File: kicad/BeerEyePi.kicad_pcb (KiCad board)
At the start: 2 copper layers, 65 x 63 mm, 72 parts, among them J1 RaspberryPi, J2 Extension, J3 RGB_LED, J4 TransSensor, J5 RGB_LED, J6 RGB_LED, J7 TransSensor, Q1 IRLML2502, Q2 IRLML2502, Q3 IRLML2502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

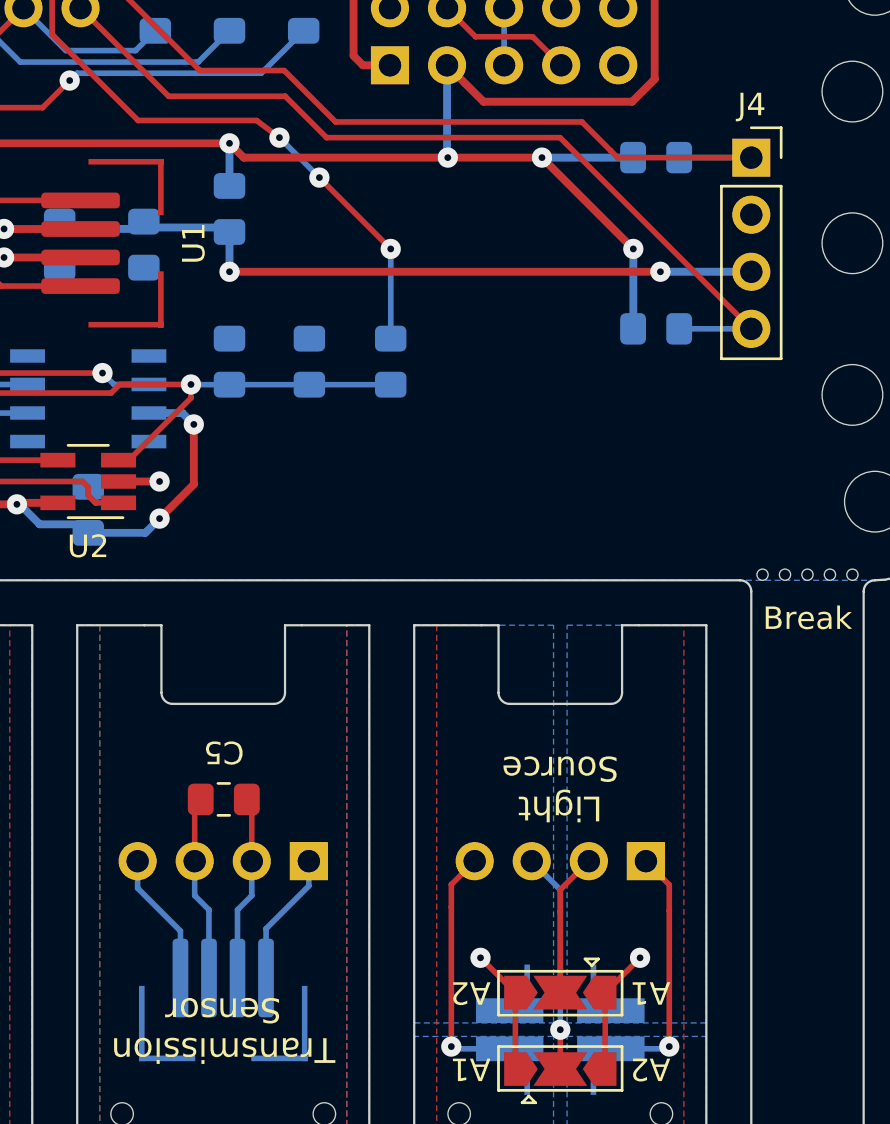
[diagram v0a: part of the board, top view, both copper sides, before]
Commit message: Fixed flawed pin socket orientation for sensor module. Generated gerber files.
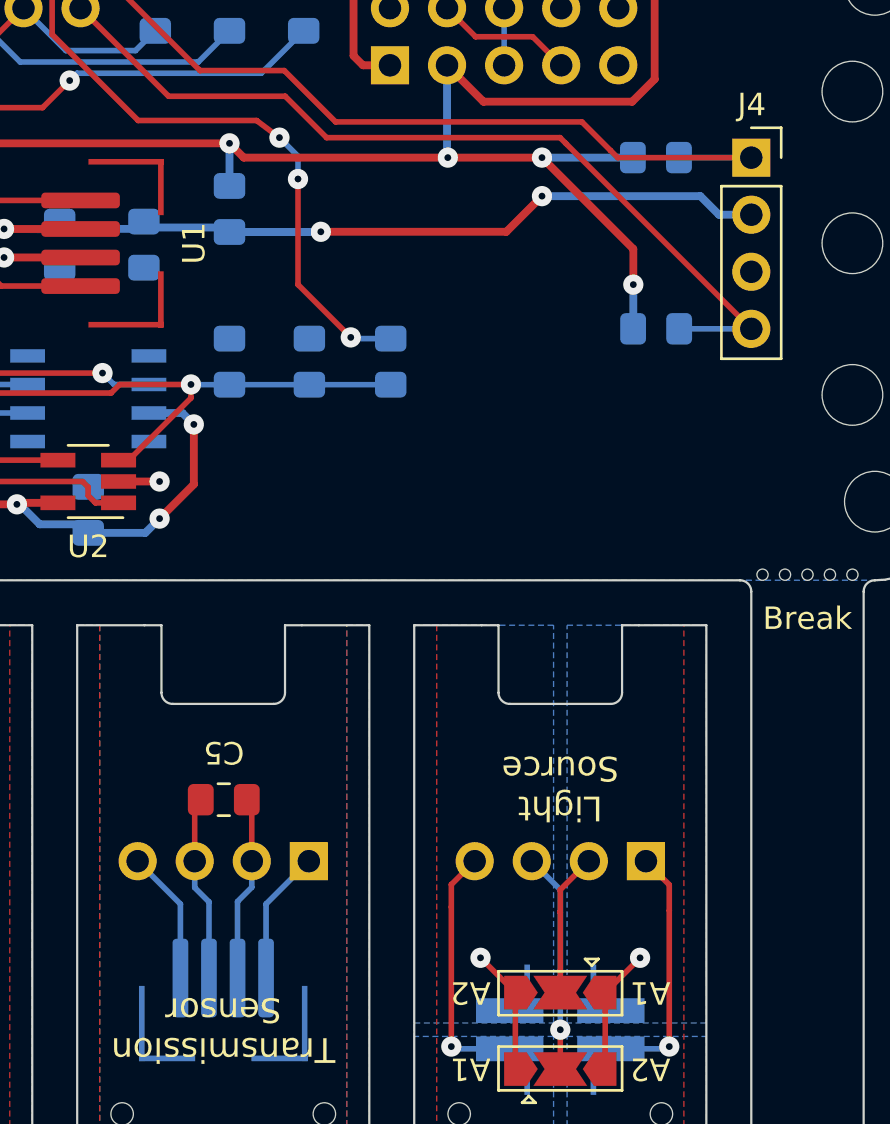
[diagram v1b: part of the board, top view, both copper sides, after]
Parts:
- moved R12 7.62 mm to (151.8, 111.2)
- moved R10 7.62 mm to (151.8, 118.8)
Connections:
- J1 pad 15: SCL1 -> SDA1
- J1 pad 16: SDA1 -> SCL1
- J4 pad 1: SDA1 -> SCL1
- J4 pad 2: GND -> +3.3VADC
- J4 pad 3: +3.3VADC -> GND
- J4 pad 4: SCL1 -> SDA1
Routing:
- net +3.3VADC: track 39.4 -> 42.7 mm
- net SDA1: track 36.9 -> 39.0 mm
- net SCL1: track 39.0 -> 36.9 mm
- net LED_CURRENT: track 29.4 -> 30.4 mm
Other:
- rule via_min_size: 0.4 -> 0.6
- board text added: "Beer Eye 0.1a rev.1 by H.-C. Ahlswede https://github.com/beer-eye"
- board text removed: "Beer Eye 0.1a rev.0 by H.-C. Ahlswede https://github.com/hcahlswede"
- board text removed: "HARWIN M20 SERIES AND SAMTEC SSW/STW ARE COMPATIBLE!!! ASSUME A BOARD TO HOLE SPACING OF 13.5mm I.E. A HOLE TO PCB EDGE SPAING OF 11.5mm!!!! HOWEVER, SAMTEC CONS ARE SLIGHTLY WIDER!!!!!! TAKE THIS INTO ACCOUNT WHEN DESIGNING THE HOLDERS!!!"
- board text removed: "Linearization of VEML7700: The VEML7700 in only strictly linear from 0...1klx with gain 1/4 and 1/8. The linearity may be tested by recording a sequence of different illumination levels. As the two sensors are placed at different positions their values differ. Hence this each sample of the sequence is approximately the derivative of the sensor response curve. This response curve can then be used 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"
- board text removed: "Min. distance between Holes: 0.45mm Min. distance between Trace and Border: 0.3mm Min. distance between Silkscreen and Soldermask: 0.3mm Min. distance between Silkscreen and Border: 0.3mm TODO: Change via drill to 0.4mm and restring ro 0.3mm TODO: Change mouse bits to 0.5mm holes and 0.5mm hole spacing"
